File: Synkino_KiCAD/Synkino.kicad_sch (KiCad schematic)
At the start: 160 parts, among them J1 Pwr, J10 EYE8_OUT, J11 EYE4_OUT, J12 Eye, J13 EYE5_OUT, J2 Eye, J3 3.5mm, J4 Micro_SD_Card_Det_Hirose_DM3AT, J5 EYE1_OUT, J6 EYE6_OUT, J7 EYE2_OUT, J8 EYE7_OUT, J9 EYE3_OUT, Q1 IRF7319, Q2 BC847 o. SS8050, Q3 IRLML2244 o. AO3401A, SW1 Power, SW2 Rotary_Encoder_Switch, SW3 Reset, U1 ME6210A50PG, U10 ATMEGA328P-AU, U11 QRE1113GR, U12 QRE1113GR, U13 QRE1113GR, U14 QRE1113GR, U15 QRE1113GR, U16 QRE1113GR, U17 24LC256, U18 QRE1113GR, U2 ATMEGA328P-AU, U3 74HC4050, U4 SPIOLED128x64, U5 AP7312-1833W6-7, U6 74HC14, U7 VS1053B, U8 GS3005, U9 QRE1113GR, X1 FTDIconn, X2 ICSP, X3 FTDIconn, X4 ICSP, Y1 16Mhz, Y2 12.288MHz, Y3 16Mhz

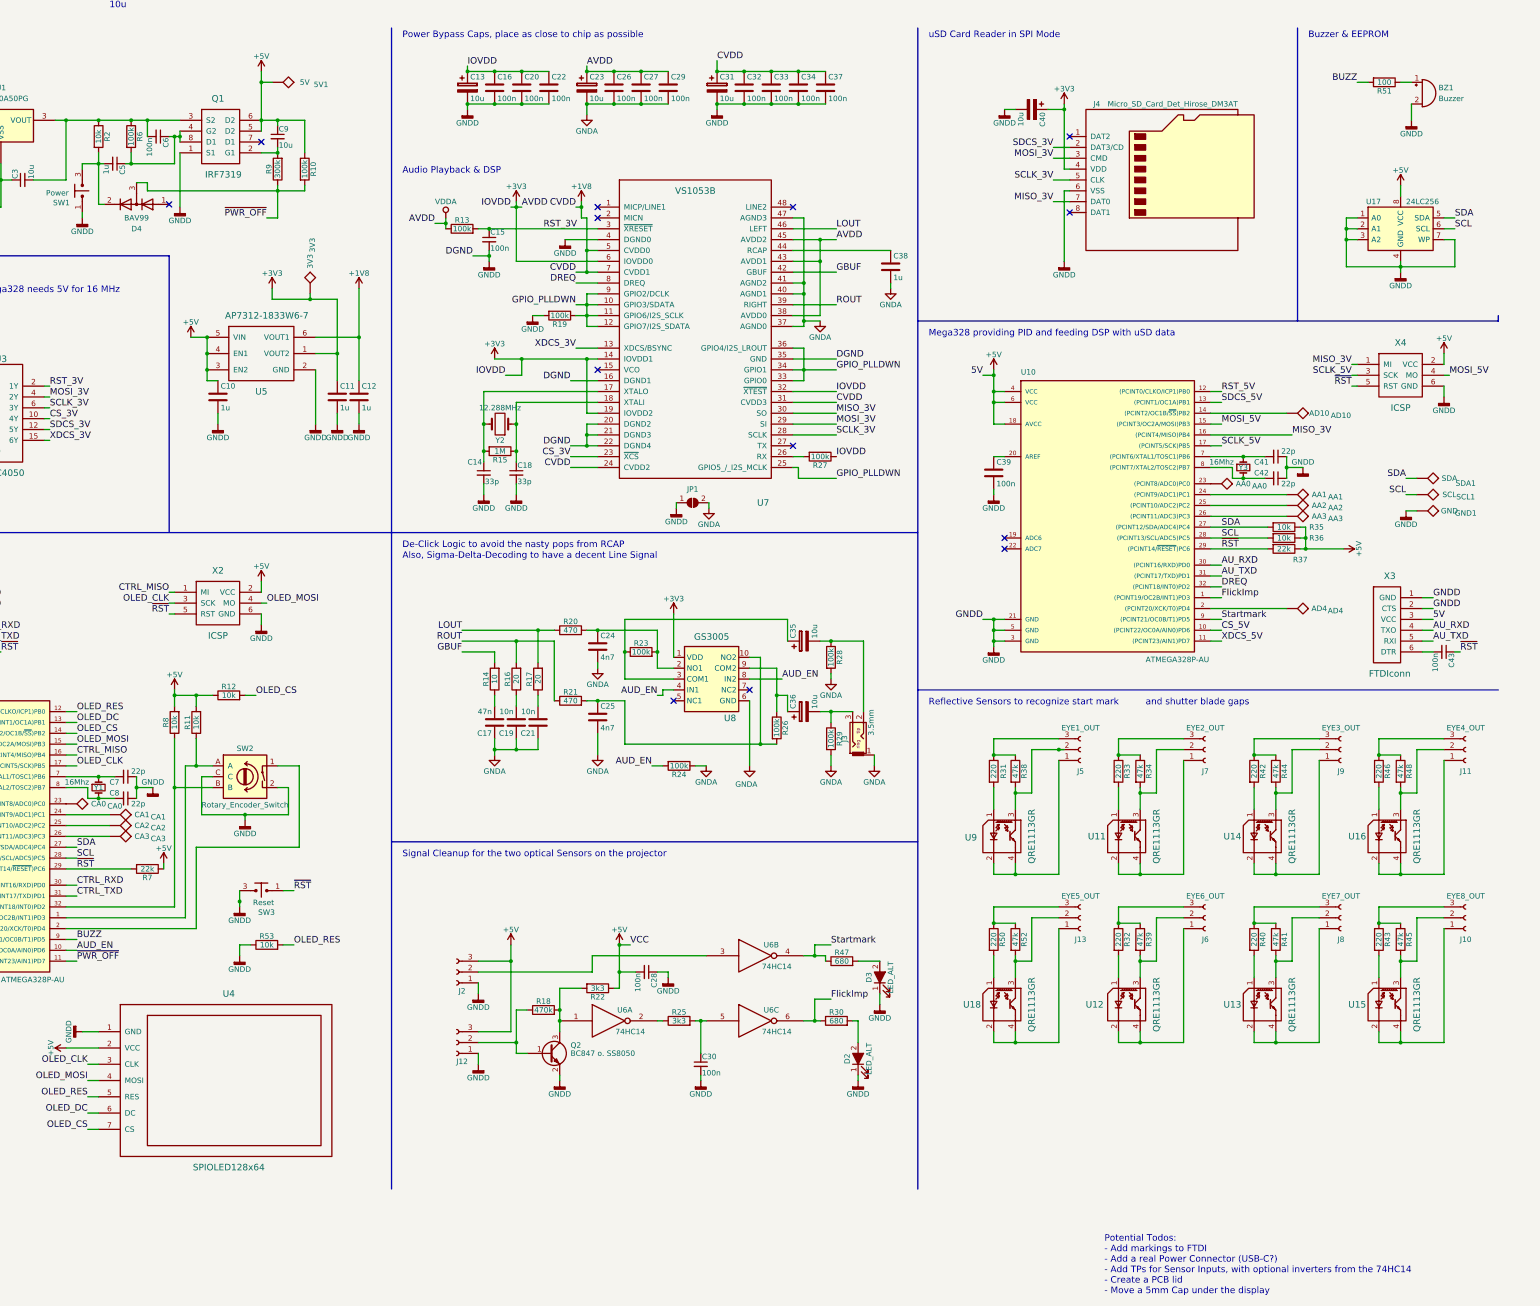
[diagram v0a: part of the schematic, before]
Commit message: Fixing TP Labels and various footprints
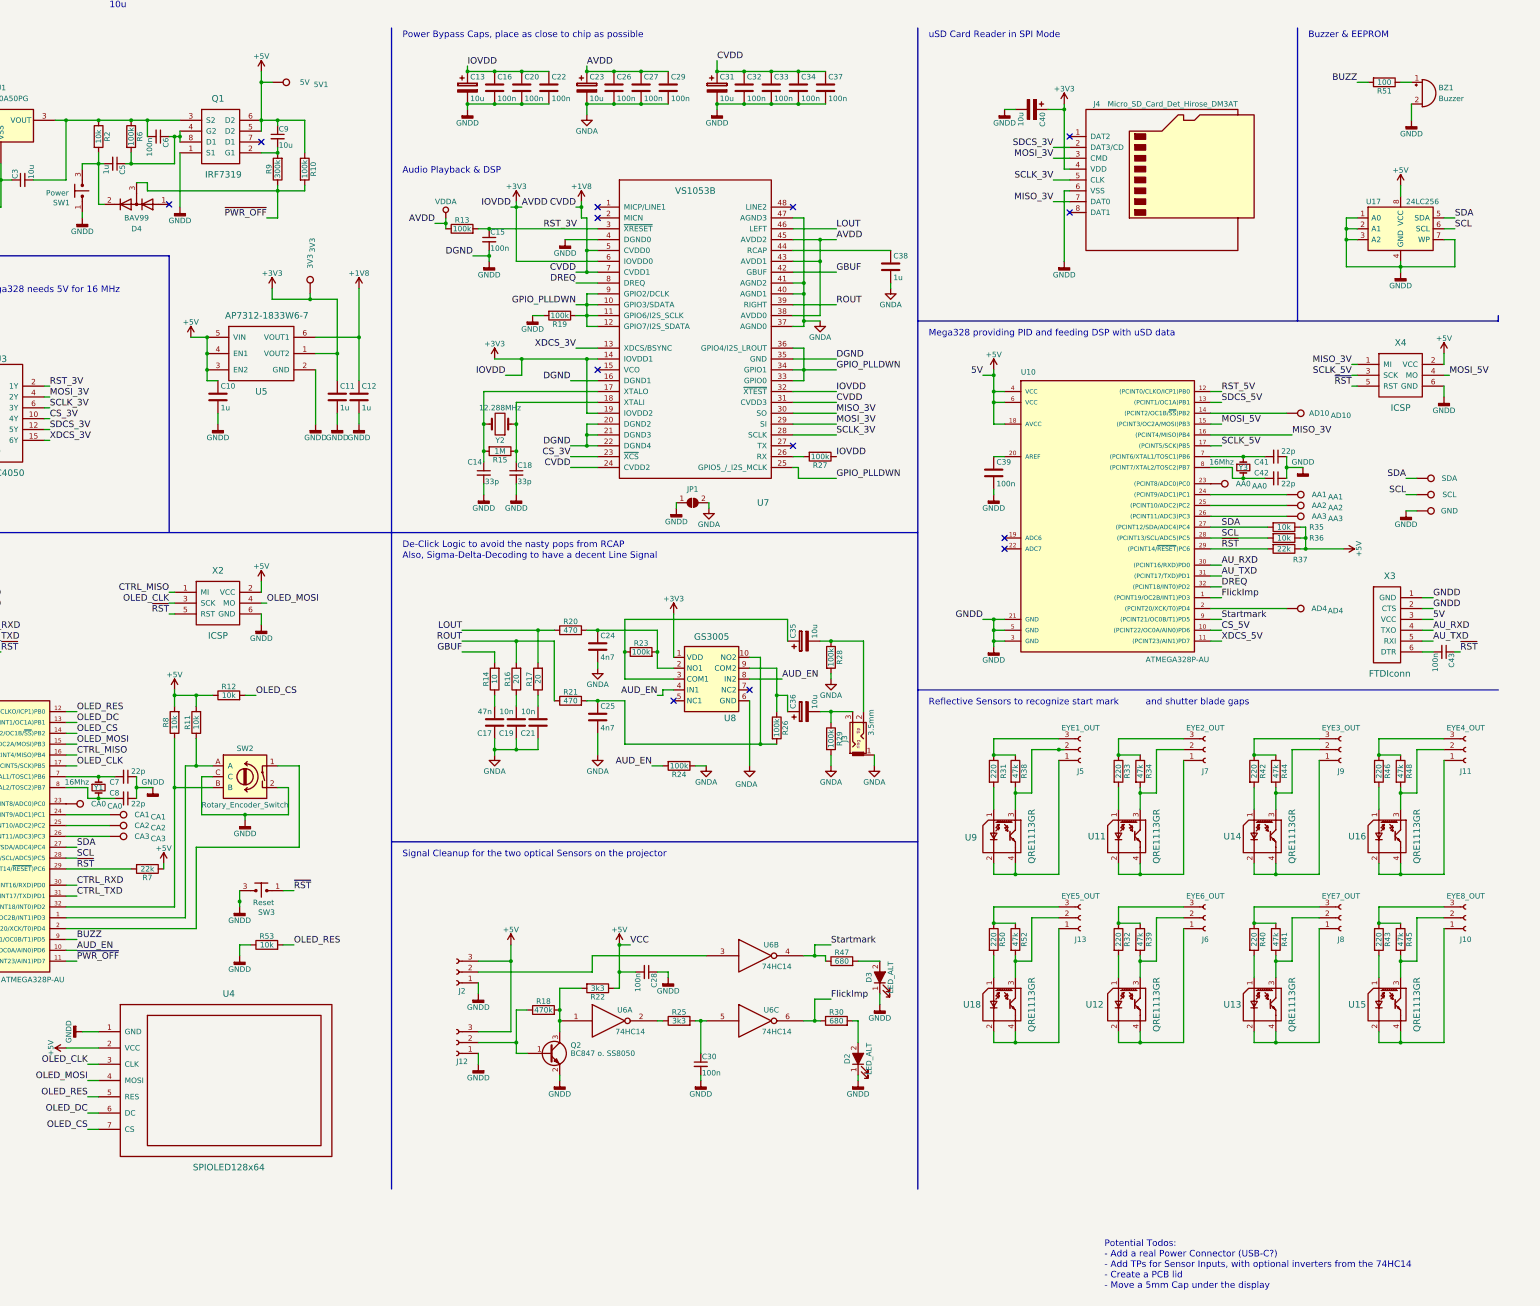
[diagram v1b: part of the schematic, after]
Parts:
- 3V3, 5V1, AA0, AA1, AA2, AA3, AD10, AD4, GND1: footprint TestPoint:TestPoint_THTPad_1.5x1.5mm_Drill0.7mm -> TestPoint:TestPoint_THTPad_1.5x1.5mm_Drill0.7mm_no_name; symbol Synkino:TEST -> Connector:TestPoint
- BZ1: footprint Peacemans_Footprints:AAC801J-13 -> easyEDA:BUZ-SMD_4P-L7.5-W7.5-BR
- CA0, CA1, CA2, CA3: footprint TestPoint:TestPoint_THTPad_D1.5mm_Drill0.7mm -> TestPoint:TestPoint_THTPad_1.5x1.5mm_Drill0.7mm_no_name; symbol Synkino:TEST -> Connector:TestPoint
- SCL1: footprint TestPoint:TestPoint_THTPad_1.5x1.5mm_Drill0.7mm -> TestPoint:TestPoint_THTPad_1.5x1.5mm_Drill0.7mm_no_name; symbol Synkino:TEST -> Connector:TestPoint; now in the parts list
- SDA1: footprint TestPoint:TestPoint_THTPad_1.5x1.5mm_Drill0.7mm -> TestPoint:TestPoint_THTPad_1.5x1.5mm_Drill0.7mm_no_name; symbol Synkino:TEST -> Connector:TestPoint_no_name; now in the parts list
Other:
- note added: "Potential Todos: - Add a real Power Connector (USB-C?) - Add TPs for Sensor Inputs, with optional inverters from the 74HC14 - Create a PCB lid - Move a 5mm Cap under the display"
- note removed: "Potential Todos: - Add markings to FTDI - Add a real Power Connector (USB-C?) - Add TPs for Sensor Inputs, with optional inverters from the 74HC14 - Create a PCB lid - Move a 5mm Cap under the display"
- moved on the sheet: 3V3, 5V1, AA0, AA1, AA2, AA3, AD10, AD4, CA0, CA1, CA2, CA3

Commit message: Footprint Updates
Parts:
- X1, X3: footprint Connector_PinHeader_2.54mm:PinHeader_1x06_P2.54mm_Vertical -> Connector_PinHeader_2.54mm:PinHeader_1x06_P2.54mm_Vertical_FTDI_displaced
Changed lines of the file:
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@@
 			)
 		)
-		(property "Footprint" "Connector_PinHeader_2.54mm:PinHeader_1x06_P2.54mm_Vertical"
+		(property "Footprint" "Connector_PinHeader_2.54mm:PinHeader_1x06_P2.54mm_Vertical_FTDI_displaced"
 			(at 382.27 151.13 0)
 			(effects
@@
 			)
 		)
-		(property "Footprint" "Connector_PinHeader_2.54mm:PinHeader_1x06_P2.54mm_Vertical"
+		(property "Footprint" "Connector_PinHeader_2.54mm:PinHeader_1x06_P2.54mm_Vertical_FTDI_displaced"
 			(at 40.64 151.13 0)
 			(effects
@@
 					(size 1.27 1.27)
 				)
+				(hide yes)
 			)
 		)

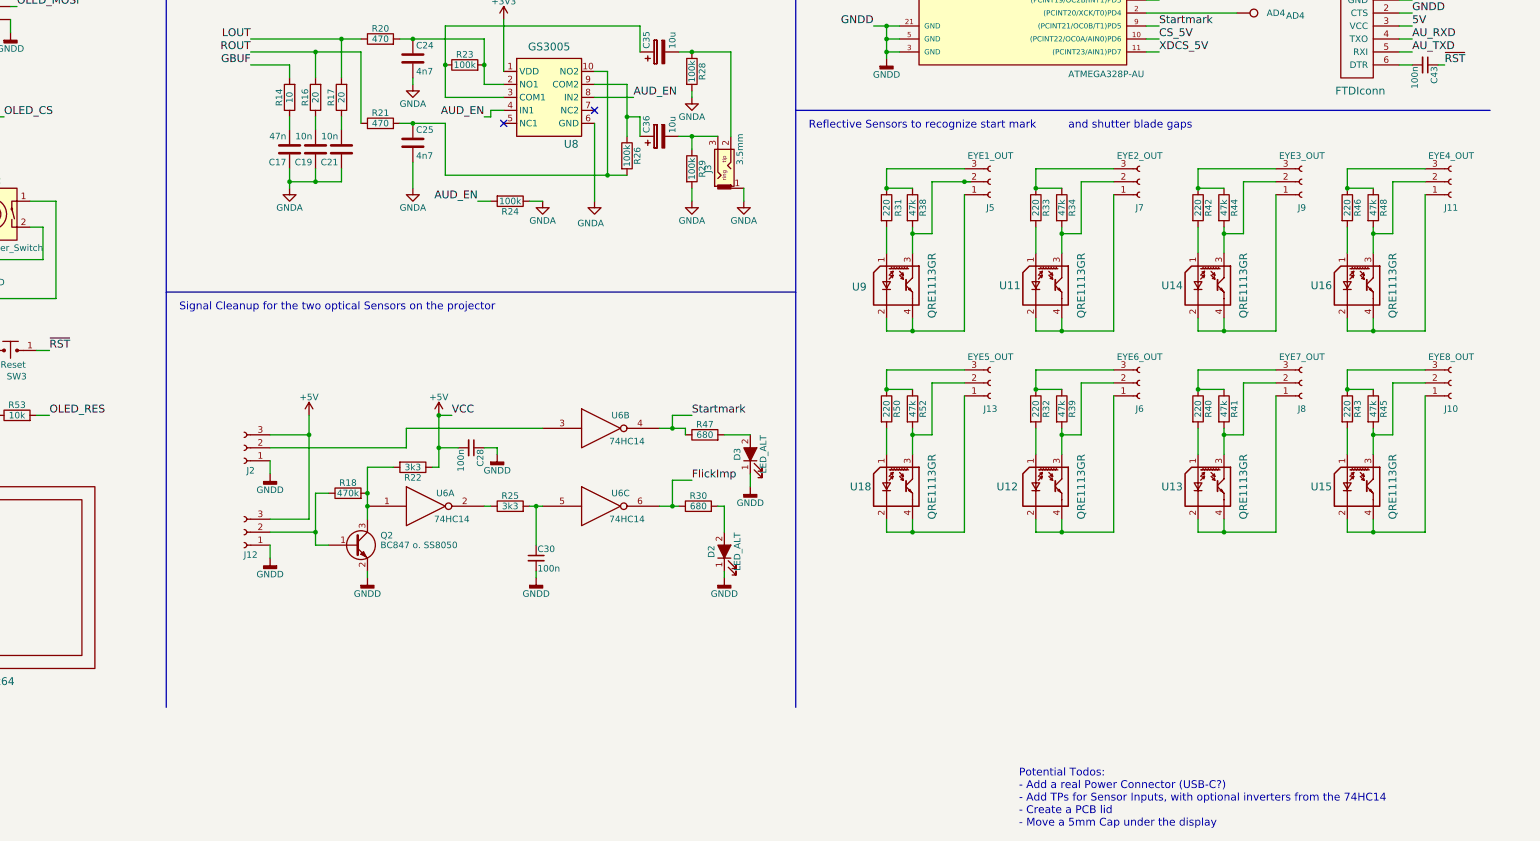
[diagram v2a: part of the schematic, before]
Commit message: Holding the OLED by a capacitor
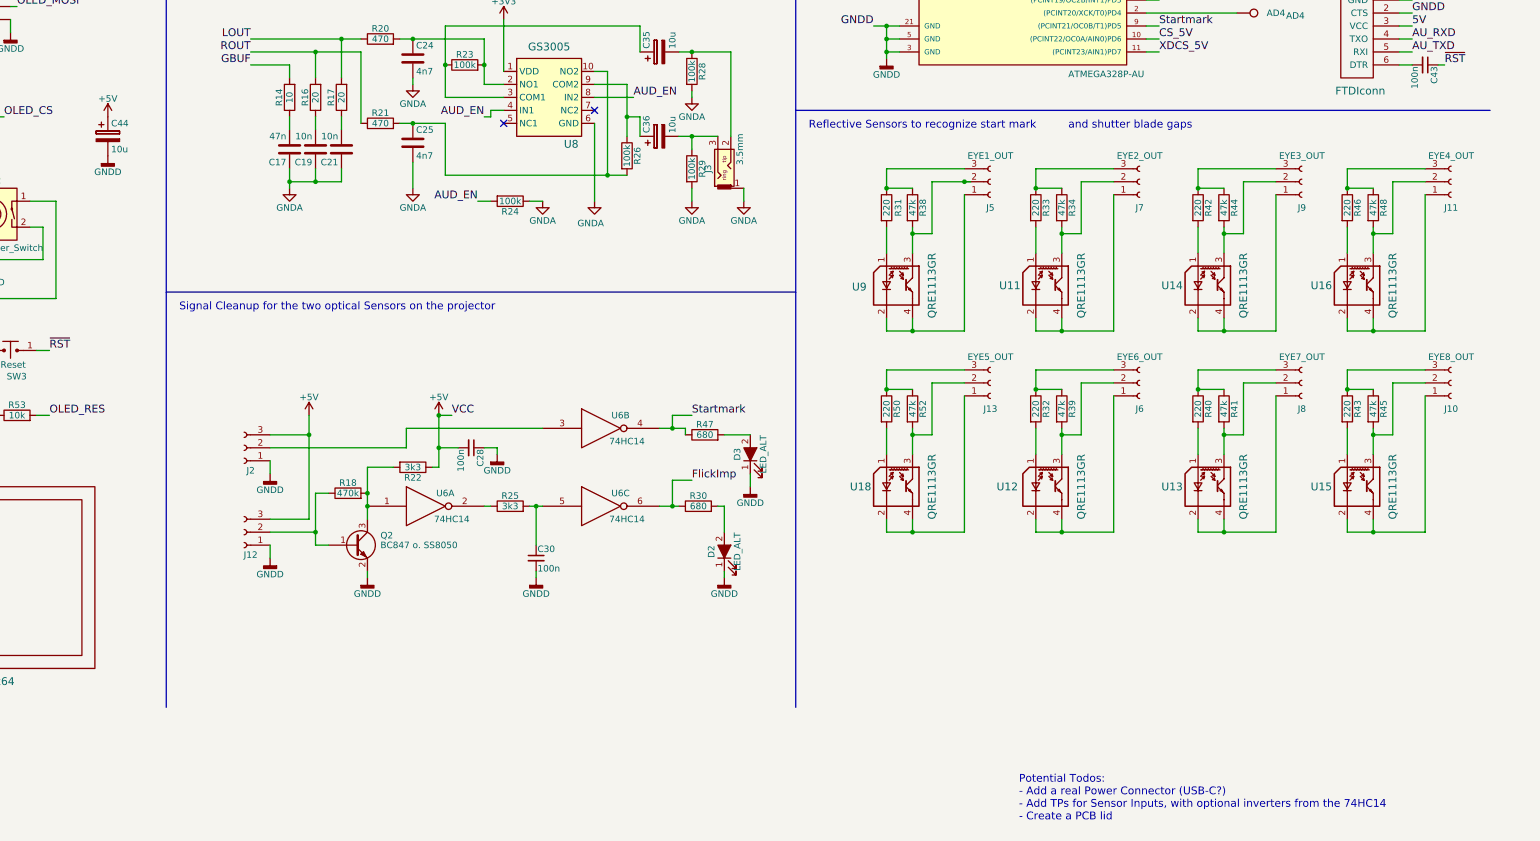
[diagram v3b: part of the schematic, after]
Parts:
- added C44: 10u, Capacitor_SMD:CP_Elec_4x5.8, symbol Synkino:CP
- Y1, Y2, Y3: footprint Peacemans_Footprints:CRYSTAL_7A -> Crystal:Crystal_SMD_5032-2Pin_5.0x3.2mm
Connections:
- net +5V: now also C44.1
- net GND: now also C44.2
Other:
- note added: "Potential Todos: - Add a real Power Connector (USB-C?) - Add TPs for Sensor Inputs, with optional inverters from the 74HC14 - Create a PCB lid"
- note removed: "Potential Todos: - Add a real Power Connector (USB-C?) - Add TPs for Sensor Inputs, with optional inverters from the 74HC14 - Create a PCB lid - Move a 5mm Cap under the display"
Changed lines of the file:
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@@
 		)
 	)
-	(text "Potential Todos:\n- Add a real Power Connector (USB-C?)\n- Add TPs for Sensor Inputs, with optional inverters from the 74HC14\n- Create a PCB lid\n- Move a 5mm Cap under the display"
+	(text "Potential Todos:\n- Add a real Power Connector (USB-C?)\n- Add TPs for Sensor Inputs, with optional inverters from the 74HC14\n- Create a PCB lid\n"
 		(exclude_from_sim no)
 		(at 315.468 302.26 0)
@@
 			)
 		)
-		(property "Footprint" "Peacemans_Footprints:CRYSTAL_7A"
+		(property "Footprint" "Crystal:Crystal_SMD_5032-2Pin_5.0x3.2mm"
 			(at 173.99 105.41 0)
 			(effects
@@
 			)
 		)
-		(property "Footprint" "Peacemans_Footprints:CRYSTAL_7A"
+		(property "Footprint" "Crystal:Crystal_SMD_5032-2Pin_5.0x3.2mm"
 			(at 80.01 190.5 0)
 			(effects
@@
 			)
 		)
-		(property "Footprint" "Peacemans_Footprints:CRYSTAL_7A"
+		(property "Footprint" "Crystal:Crystal_SMD_5032-2Pin_5.0x3.2mm"
 			(at 347.98 115.57 0)
 			(effects
@@
 	)
 	(symbol
+		(lib_id "Synkino:CP")
+		(at 137.16 172.72 0)
+		(unit 1)
+		(exclude_from_sim no)
+		(in_bom yes)
+		(on_board yes)
+		(dnp no)
+		(property "Reference" "C44"
+			(at 137.795 170.18 0)
+			(effects
+				(font
+					(size 1.27 1.27)
+				)
+				(justify left)
+			)
+		)
+		(property "Value" "10u"
+			(at 137.795 175.26 0)
+			(effects
+				(font
+					(size 1.27 1.27)
+				)
+				(justify left)
+			)
+		)
+		(property "Footprint" "Capacitor_SMD:CP_Elec_4x5.8"
+			(at 138.1252 176.53 0)
+			(effects
+				(font
+					(size 1.27 1.27)
+				)
+				(hide yes)
+			)
+		)
+		(property "Datasheet" ""
+			(at 137.16 172.72 0)
+			(effects
+				(font
+					(size 1.27 1.27)
+				)
+				(hide yes)
+			)
+		)
+		(property "Description" ""
+			(at 137.16 172.72 0)
+			(effects
+				(font
+					(size 1.27 1.27)
+				)
+				(hide yes)
+			)
+		)
+		(property "Inventory" "E"
+			(at 137.16 172.72 0)
+			(effects
+				(font
+					(size 1.27 1.27)
+				)
+				(hide yes)
+			)
+		)
+		(property "LCSC" "C249817"
+			(at 137.16 172.72 0)
+			(effects
+				(font
+					(size 1.27 1.27)
+				)
+				(hide yes)
+			)
+		)
+		(pin "1"
+		)
+		(pin "2"
+		)
+		(instances
+			(project "Synkino"
+				(path "/9d4924d9-a2ad-42f2-a951-8d7a9cc74761"
+					(reference "C44")
+					(unit 1)
+				)
+			)
+		)
+	)
+	(symbol
+		(lib_id "Synkino:+5V")
+		(at 137.16 168.91 0)
+		(unit 1)
+		(exclude_from_sim no)
+		(in_bom yes)
+		(on_board yes)
+		(dnp no)
+		(property "Reference" "#PWR079"
+			(at 137.16 172.72 0)
+			(effects
+				(font
+					(size 1.27 1.27)
+				)
+				(hide yes)
+			)
+		)
+		(property "Value" "+5V"
+			(at 137.16 165.354 0)
+			(effects
+				(font
+					(size 1.27 1.27)
+				)
+			)
+		)
+		(property "Footprint" ""
+			(at 137.16 168.91 0)
+			(effects
+				(font
+					(size 1.27 1.27)
+				)
+				(hide yes)
+			)
+		)
+		(property "Datasheet" ""
+			(at 137.16 168.91 0)
+			(effects
+				(font
+					(size 1.27 1.27)
+				)
+				(hide yes)
+			)
+		)
+		(property "Description" ""
+			(at 137.16 168.91 0)
+			(effects
+				(font
+					(size 1.27 1.27)
+				)
+				(hide yes)
+			)
+		)
+		(pin "1"
+		)
+		(instances
+			(project "Synkino"
+				(path "/9d4924d9-a2ad-42f2-a951-8d7a9cc74761"
+					(reference "#PWR079")
+					(unit 1)
+				)
+			)
+		)
+	)
+	(symbol
 		(lib_id "Diode:BAV99")
 		(at 88.9 53.975 180)
@@
 					(unit 1)
 				)
+			)
+		)
+	)
+	(symbol
+		(lib_id "Synkino:GNDD")
+		(at 137.16 176.53 0)
+		(unit 1)
+		(exclude_from_sim no)
+		(in_bom yes)
+		(on_board yes)
+		(dnp no)
+		(property "Reference" "#PWR067"
+			(at 137.16 182.88 0)
+			(effects
+				(font
+					(size 1.27 1.27)
+				)
+				(hide yes)
+			)
+		)
+		(property "Value" "GNDD"
+			(at 137.16 179.705 0)
+			(effects
+				(font
+					(size 1.27 1.27)
+				)
+			)
+		)
+		(property "Footprint" ""
+			(at 137.16 176.53 0)
+			(effects
+				(font
+					(size 1.27 1.27)
+				)
+				(hide yes)
+			)
+		)
+		(property "Datasheet" ""
+			(at 137.16 176.53 0)
+			(effects
+				(font
+					(size 1.27 1.27)
+				)
+				(hide yes)
+			)
+		)
+		(property "Description" ""
+			(at 137.16 176.53 0)
+			(effects
+				(font
+					(size 1.27 1.27)
+				)
+				(hide yes)
+			)
+		)
+		(pin "1"
+		)
+		(instances
+			(project "Synkino"
+				(path "/9d4924d9-a2ad-42f2-a951-8d7a9cc74761"
+					(reference "#PWR067")
+					(unit 1)
+				)
